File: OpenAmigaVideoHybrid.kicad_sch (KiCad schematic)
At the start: 64 parts, among them J1 Conn_01x22, Q1 MMBT3904, Q2 MMBT3904, Q3 MMBT3904, Q4 MMBT3904, Q5 MMBT3904, Q6 S9012

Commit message: work done
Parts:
- J1: footprint Connector_PinHeader_2.54mm:PinHeader_1x22_P2.54mm_Vertical -> OpenAmigaVideoHybrid:side_connector
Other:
- note added: "According to the documentation I could find, VID and VCC are not connected on the -03 revision. Closing this jumper will bridge them anyway as on many other Hybrid remakes."
- note removed: "According to documentation I could find, VID and VCC are not connected on -03 revision. Closing this jumper will bridge them as on other Vidiot remakes."
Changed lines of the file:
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@@
 		)
 	)
-	(text "According to documentation I could \nfind, VID and VCC are not connected \non -03 revision. Closing this jumper\nwill bridge them as on other Vidiot\nremakes."
+	(text "According to the documentation I could \nfind, VID and VCC are not connected \non the -03 revision. Closing this jumper\nwill bridge them anyway as on many other \nHybrid remakes."
 		(exclude_from_sim no)
 		(at 184.785 38.1 0)
@@
 			)
 		)
-		(property "Footprint" "Connector_PinHeader_2.54mm:PinHeader_1x22_P2.54mm_Vertical"
+		(property "Footprint" "OpenAmigaVideoHybrid:side_connector"
 			(at 25.4 91.44 0)
 			(effects

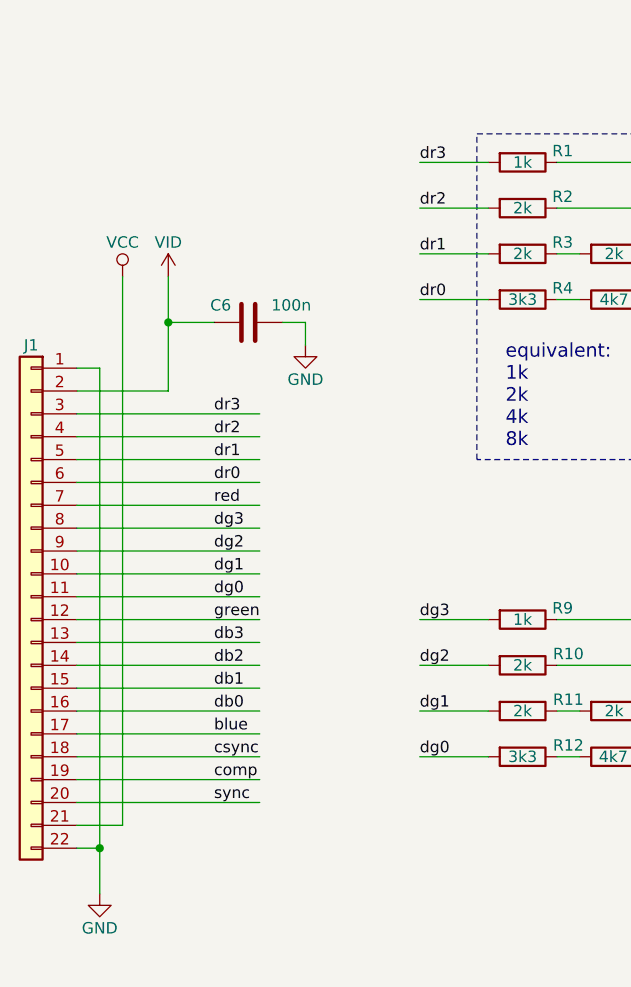
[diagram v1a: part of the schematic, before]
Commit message: routing done
DRC pass
added fiducials and silkscreen
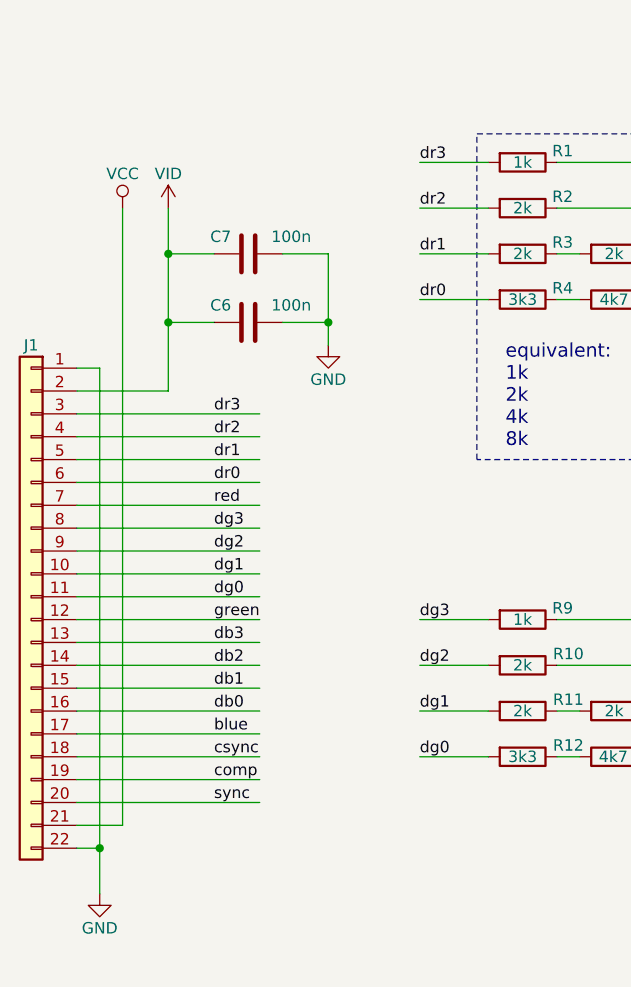
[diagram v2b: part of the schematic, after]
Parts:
- added C7: 100n, Capacitor_SMD:C_0603_1608Metric, symbol OpenAmigaVideoHybrid-rescue:C
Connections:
- net GND: now also C7.2
- net VID: now also C7.1
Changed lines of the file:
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@@
 	)
 	(junction
+		(at 58.42 60.96)
+		(diameter 0)
+		(color 0 0 0 0)
+	)
+	(junction
 		(at 233.68 83.82)
 		(diameter 0)
@@
 	)
 	(junction
+		(at 40.64 53.34)
+		(diameter 0)
+		(color 0 0 0 0)
+	)
+	(junction
 		(at 205.74 116.84)
 		(diameter 0)
@@
 	(wire
 		(pts
+			(xy 40.64 53.34) (xy 40.64 60.96)
+		)
+		(stroke
+			(width 0)
+			(type default)
+		)
+	)
+	(wire
+		(pts
 			(xy 233.68 139.7) (xy 233.68 142.24)
 		)
@@
 	(wire
 		(pts
-			(xy 35.56 55.88) (xy 35.56 116.84)
+			(xy 35.56 48.26) (xy 35.56 116.84)
 		)
 		(stroke
@@
 	(wire
 		(pts
+			(xy 40.64 53.34) (xy 45.72 53.34)
+		)
+		(stroke
+			(width 0)
+			(type default)
+		)
+	)
+	(wire
+		(pts
 			(xy 104.14 93.98) (xy 114.3 93.98)
 		)
@@
 	(wire
 		(pts
+			(xy 53.34 53.34) (xy 58.42 53.34)
+		)
+		(stroke
+			(width 0)
+			(type default)
+		)
+	)
+	(wire
+		(pts
 			(xy 170.18 63.5) (xy 170.18 116.84)
 		)
@@
 	(wire
 		(pts
+			(xy 58.42 53.34) (xy 58.42 60.96)
+		)
+		(stroke
+			(width 0)
+			(type default)
+		)
+	)
+	(wire
+		(pts
 			(xy 218.44 104.14) (xy 218.44 106.68)
 		)
@@
 	(wire
 		(pts
-			(xy 55.88 60.96) (xy 55.88 63.5)
+			(xy 58.42 60.96) (xy 58.42 63.5)
 		)
 		(stroke
@@
 	(wire
 		(pts
-			(xy 53.34 60.96) (xy 55.88 60.96)
+			(xy 53.34 60.96) (xy 58.42 60.96)
 		)
 		(stroke
@@
 	(wire
 		(pts
-			(xy 40.64 55.88) (xy 40.64 60.96)
+			(xy 40.64 48.26) (xy 40.64 53.34)
 		)
 		(stroke
@@
 		(lib_name "VCC_10")
 		(lib_id "OpenAmigaVideoHybrid-rescue:VCC")
-		(at 35.56 55.88 0)
+		(at 35.56 48.26 0)
 		(unit 1)
 		(exclude_from_sim no)
@@
 		(dnp no)
 		(property "Reference" "#PWR02"
-			(at 35.56 59.69 0)
+			(at 35.56 52.07 0)
 			(effects
 				(font
@@
 		)
 		(property "Value" "VCC"
-			(at 35.56 52.07 0)
+			(at 35.56 44.45 0)
 			(effects
 				(font
@@
 		)
 		(property "Footprint" ""
-			(at 35.56 55.88 0)
+			(at 35.56 48.26 0)
 			(effects
 				(font
@@
 		)
 		(property "Datasheet" ""
-			(at 35.56 55.88 0)
+			(at 35.56 48.26 0)
 			(effects
 				(font
@@
 		)
 		(property "Description" ""
-			(at 35.56 55.88 0)
+			(at 35.56 48.26 0)
 			(effects
 				(font
@@
 		(lib_name "GND_9")
 		(lib_id "OpenAmigaVideoHybrid-rescue:GND")
-		(at 55.88 63.5 0)
+		(at 58.42 63.5 0)
 		(unit 1)
 		(exclude_from_sim no)
@@
 		(dnp no)
 		(property "Reference" "#PWR017"
-			(at 55.88 69.85 0)
+			(at 58.42 69.85 0)
 			(effects
 				(font
@@
 		)
 		(property "Value" "GND"
-			(at 55.88 67.31 0)
+			(at 58.42 67.31 0)
 			(effects
 				(font
@@
 		)
 		(property "Footprint" ""
-			(at 55.88 63.5 0)
+			(at 58.42 63.5 0)
 			(effects
 				(font
@@
 		)
 		(property "Datasheet" ""
-			(at 55.88 63.5 0)
+			(at 58.42 63.5 0)
 			(effects
 				(font
@@
 		)
 		(property "Description" ""
-			(at 55.88 63.5 0)
+			(at 58.42 63.5 0)
 			(effects
 				(font
@@
 	)
 	(symbol
+		(lib_name "C_10")
+		(lib_id "OpenAmigaVideoHybrid-rescue:C")
+		(at 49.53 53.34 90)
+		(unit 1)
+		(exclude_from_sim no)
+		(in_bom yes)
+		(on_board yes)
+		(dnp no)
+		(property "Reference" "C7"
+			(at 47.625 51.435 90)
+			(effects
+				(font
+					(size 1.27 1.27)
+				)
+				(justify left)
+			)
+		)
+		(property "Value" "100n"
+			(at 56.515 51.435 90)
+			(effects
+				(font
+					(size 1.27 1.27)
+				)
+				(justify left)
+			)
+		)
+		(property "Footprint" "Capacitor_SMD:C_0603_1608Metric"
+			(at 53.34 52.3748 0)
+			(effects
+				(font
+					(size 1.27 1.27)
+				)
+				(hide yes)
+			)
+		)
+		(property "Datasheet" ""
+			(at 49.53 53.34 0)
+			(effects
+				(font
+					(size 1.27 1.27)
+				)
+				(hide yes)
+			)
+		)
+		(property "Description" ""
+			(at 49.53 53.34 0)
+			(effects
+				(font
+					(size 1.27 1.27)
+				)
+			)
+		)
+		(property "LCSC Part #" ""
+			(at 49.53 53.34 0)
+			(effects
+				(font
+					(size 1.27 1.27)
+				)
+				(hide yes)
+			)
+		)
+		(pin "1"
+		)
+		(pin "2"
+		)
+		(instances
+			(project "OpenAmigaVideoHybrid"
+				(path "/5c56992e-e4b0-4cb0-9cef-7d9c11c14f78"
+					(reference "C7")
+					(unit 1)
+				)
+			)
+		)
+	)
+	(symbol
 		(lib_name "VCC_10")
 		(lib_id "OpenAmigaVideoHybrid-rescue:VCC")
@@
 	(symbol
 		(lib_id "power:VDC")
-		(at 40.64 55.88 0)
+		(at 40.64 48.26 0)
 		(unit 1)
 		(exclude_from_sim no)
@@
 		(dnp no)
 		(property "Reference" "#PWR015"
-			(at 40.64 59.69 0)
+			(at 40.64 52.07 0)
 			(effects
 				(font
@@
 		)
 		(property "Value" "VID"
-			(at 40.64 52.07 0)
+			(at 40.64 44.45 0)
 			(effects
 				(font
@@
 		)
 		(property "Footprint" ""
-			(at 40.64 55.88 0)
+			(at 40.64 48.26 0)
 			(effects
 				(font
@@
 		)
 		(property "Datasheet" ""
-			(at 40.64 55.88 0)
+			(at 40.64 48.26 0)
 			(effects
 				(font
@@
 		)
 		(property "Description" "Power symbol creates a global label with name \"VDC\""
-			(at 40.64 55.88 0)
+			(at 40.64 48.26 0)
 			(effects
 				(font

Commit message: designators renumbered
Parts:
- renumbered C7 to C1, C6 to C2, C1 to C3, C2 to C4, C3 to C5, C4 to C6, C5 to C7, Q5 to Q4, Q4 to Q5, R18 to R10, R19 to R11, R20 to R12, R40 to R13, R45 to R14, R41 to R15, R44 to R16, R42 to R17, R43 to R18, R5 to R19, R6 to R20, R13 to R21, R14 to R22, R21 to R23, R22 to R24, R7 to R25, R15 to R26, R23 to R27, R8 to R28, R16 to R29, R24 to R30, R47 to R35, R49 to R36, R48 to R37, R46 to R38, R30 to R39, R50 to R40, R35 to R41, R26 to R42, R25 to R43, R27 to R44, R36 to R45, R28 to R46, R37 to R47, R38 to R48, R29 to R49, R9 to R5, R39 to R50, R10 to R6, R11 to R7, R12 to R8, R17 to R9

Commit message: updated BOM for assembly by JLCPCB
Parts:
- C1, C2, C3, C4, C5, C6, C7: LCSC Part # (none) -> C14663
- J1, JP1: now left out of the parts list
- R31, R34: LCSC Part # (none) -> C23147
- R32: LCSC Part # (none) -> C25804
- R33: LCSC Part # (none) -> C23189
- R35, R38: LCSC Part # (none) -> C22843
- R39: LCSC Part # (none) -> C23265
- R41: LCSC Part # (none) -> C22809
- R45: LCSC Part # C22962 -> C22966
- R47, R48: LCSC Part # (none) -> C23140
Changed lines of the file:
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@@
 		(unit 1)
 		(exclude_from_sim no)
-		(in_bom yes)
+		(in_bom no)
 		(on_board yes)
 		(dnp no)
@@
 			)
 		)
-		(property "LCSC Part #" ""
+		(property "LCSC Part #" "C14663"
 			(at 139.7 41.91 0)
 			(effects
@@
 			)
 		)
-		(property "LCSC Part #" ""
+		(property "LCSC Part #" "C14663"
 			(at 139.7 92.71 0)
 			(effects
@@
 			)
 		)
-		(property "LCSC Part #" ""
+		(property "LCSC Part #" "C14663"
 			(at 139.7 143.51 0)
 			(effects
@@
 			)
 		)
-		(property "LCSC Part #" ""
+		(property "LCSC Part #" "C25804"
 			(at 179.07 121.92 90)
 			(effects
@@
 			)
 		)
-		(property "LCSC Part #" ""
+		(property "LCSC Part #" "C23189"
 			(at 179.07 127 90)
 			(effects
@@
 			)
 		)
-		(property "LCSC Part #" ""
+		(property "LCSC Part #" "C23147"
 			(at 179.07 132.08 90)
 			(effects
@@
 			)
 		)
-		(property "LCSC Part #" "C22962"
+		(property "LCSC Part #" "C22966"
 			(at 218.44 110.49 90)
 			(effects
@@
 			)
 		)
-		(property "LCSC Part #" ""
+		(property "LCSC Part #" "C22809"
 			(at 205.74 148.59 90)
 			(effects
@@
 			)
 		)
-		(property "LCSC Part #" ""
+		(property "LCSC Part #" "C23140"
 			(at 233.68 133.35 90)
 			(effects
@@
 			)
 		)
-		(property "LCSC Part #" ""
+		(property "LCSC Part #" "C14663"
 			(at 248.92 115.57 0)
 			(effects
@@
 			)
 		)
-		(property "LCSC Part #" ""
+		(property "LCSC Part #" "C14663"
 			(at 248.92 62.23 0)
 			(effects
@@
 			)
 		)
-		(property "LCSC Part #" ""
+		(property "LCSC Part #" "C23265"
 			(at 205.74 110.49 90)
 			(effects
@@
 			)
 		)
-		(property "LCSC Part #" ""
+		(property "LCSC Part #" "C23140"
 			(at 233.68 146.05 90)
 			(effects
@@
 			)
 		)
-		(property "LCSC Part #" ""
+		(property "LCSC Part #" "C14663"
 			(at 49.53 53.34 0)
 			(effects
@@
 			)
 		)
-		(property "LCSC Part #" ""
+		(property "LCSC Part #" "C22843"
 			(at 189.23 116.84 90)
 			(effects
@@
 			)
 		)
-		(property "LCSC Part #" ""
+		(property "LCSC Part #" "C14663"
 			(at 49.53 60.96 0)
 			(effects
@@
 			)
 		)
-		(property "LCSC Part #" ""
+		(property "LCSC Part #" "C23147"
 			(at 179.07 116.84 90)
 			(effects
@@
 			)
 		)
-		(property "LCSC Part #" ""
+		(property "LCSC Part #" "C22843"
 			(at 189.23 132.08 90)
 			(effects
@@
 		(unit 1)
 		(exclude_from_sim no)
-		(in_bom yes)
+		(in_bom no)
 		(on_board yes)
 		(dnp no)
